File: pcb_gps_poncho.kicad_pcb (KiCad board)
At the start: 2 copper layers, 41.9 x 61 mm, 9 parts, among them P1 CONN_5, P2 CONN_4

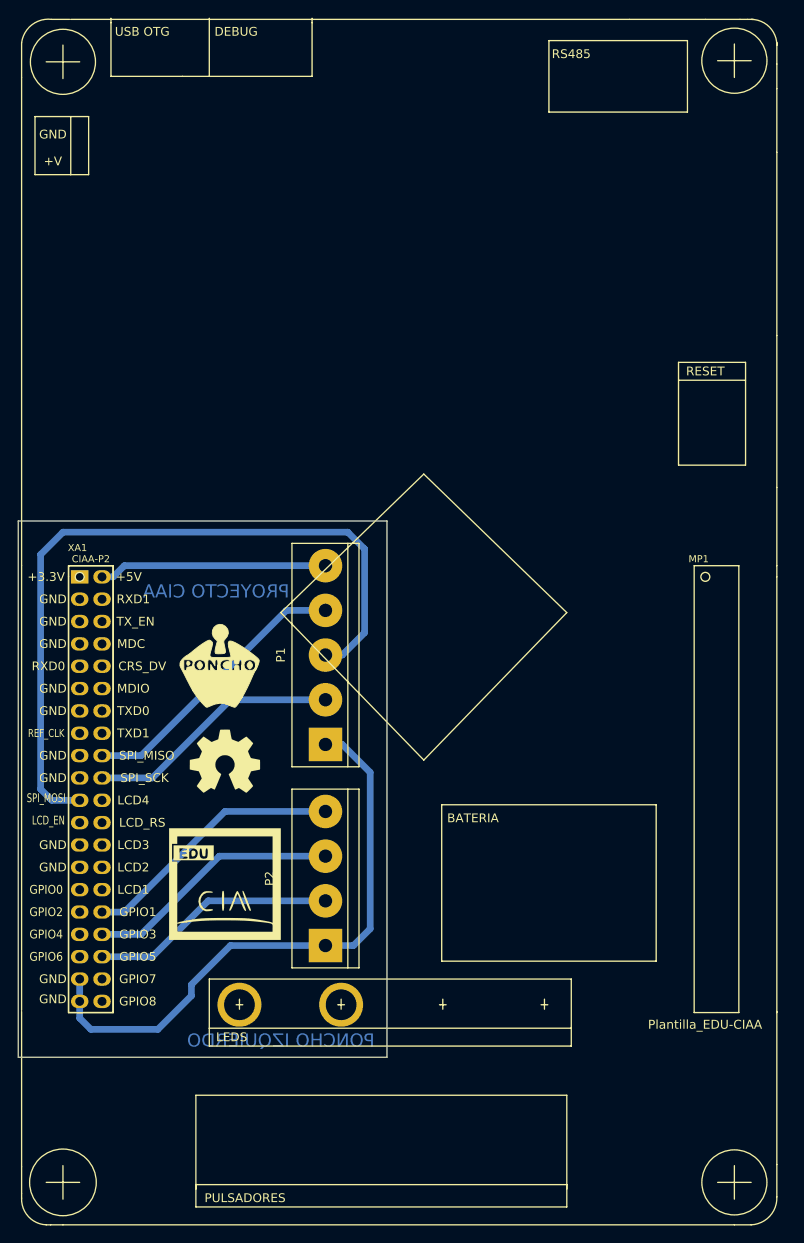
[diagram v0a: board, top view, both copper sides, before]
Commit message: Cambio de chip gps y modelo de poncho
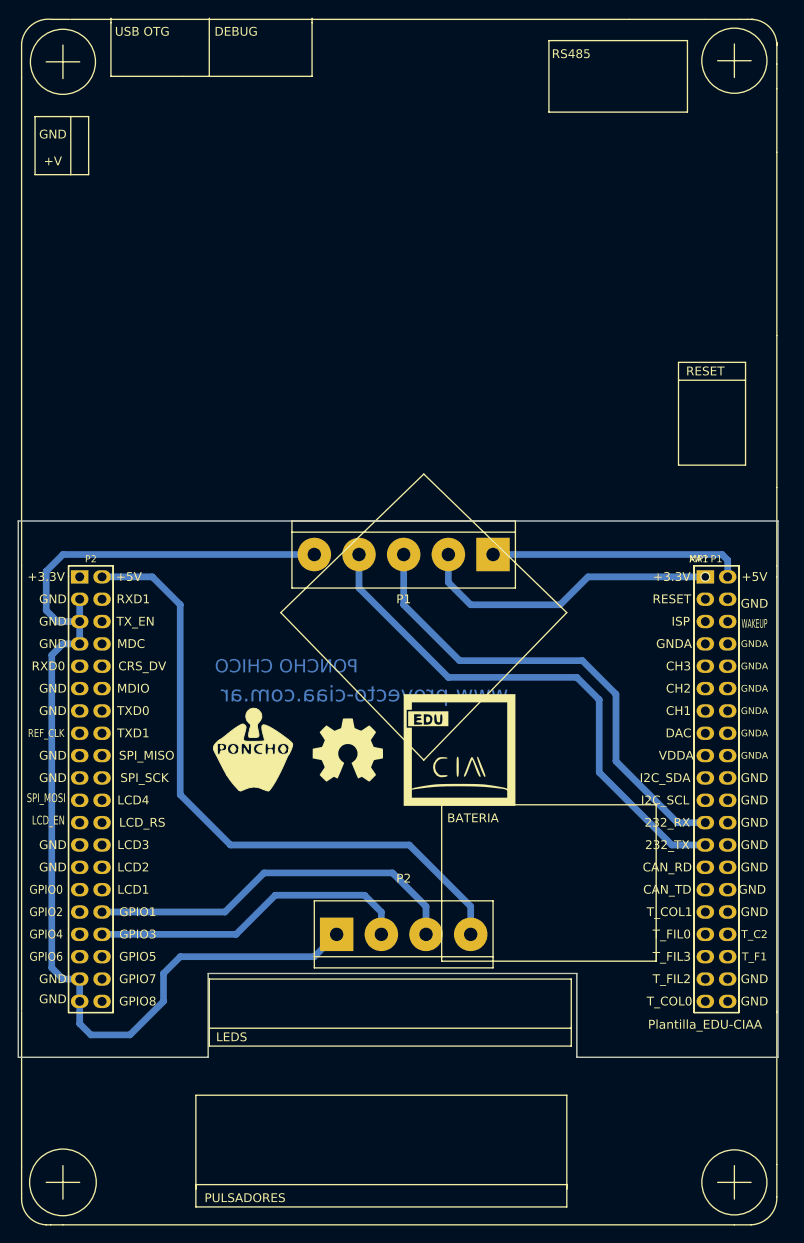
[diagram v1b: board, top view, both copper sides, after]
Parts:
- removed H1, H2: PCB_HOLE, Poncho_Modelos:Led_Hole
- removed MP1: Plantilla_EDU-CIAA, Poncho_Esqueleto:Plantilla_EDU-CIAA
- added MP?: Plantilla_EDU-CIAA, Poncho_Esqueleto:Plantilla_EDU-CIAA, F.Cu at (142.2, 81.3)
- XA1: footprint Poncho_Esqueleto:Conn_Poncho_Izquierdo -> Poncho_Esqueleto:Conn_Poncho_Chico
- moved XA1 71.1 mm to (142.2, 81.3)
- moved G*** 30.7 mm to (114.3, 101.0)
- moved P1 14.5 mm to (108.0, 78.7), turned to 180 degrees
- moved G101 14.0 mm to (101.6, 101.0)
- moved P2 10.9 mm to (108.0, 121.9), turned to 0 degrees
- moved G*** 10.3 mm to (90.8, 101.0)
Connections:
- P1 pad 1: GND -> +5V
- P1 pad 2: Net-(P1-Pad2) -> +3.3V
- P1 pad 5: +5VP -> GND
- P2 pad 4: Net-(P2-Pad4) -> +5VP
- XA1 pad 43: (no net) -> GND
- XA1 pad 45: (no net) -> GND
- XA1 pad 47: (no net) -> GND
- XA1 pad 58: Net-(P1-Pad4) -> (no net)
- XA1 pad 60: Net-(P1-Pad2) -> (no net)
- XA1 pad 61: Net-(P1-Pad3) -> (no net)
- XA1 pad 72: Net-(P2-Pad4) -> Net-(P2-Pad3)
- XA1 pad 74: Net-(P2-Pad3) -> Net-(P2-Pad2)
- XA1 pad 76: Net-(P2-Pad2) -> (no net)
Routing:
- net GND: track 67.6 -> 130.8 mm
- net +5VP: track 25.9 -> 73.3 mm
- net +3.3V: track 0.00 -> 34.8 mm
- net Net-(P1-Pad3): track 85.3 -> 54.7 mm
- net Net-(P2-Pad4): track 30.1 -> 0.00 mm
- net Net-(P1-Pad2): track 29.1 -> 0.00 mm
- net +5V: track 0.00 -> 28.8 mm
- net Net-(P1-Pad4): track 32.2 -> 60.1 mm
- net Net-(P2-Pad3): track 29.1 -> 43.4 mm
- net Net-(P2-Pad2): track 28.0 -> 36.9 mm
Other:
- board size 41.9 x 61 mm -> 86.4 x 61 mm
- board text added: "PONCHO CHICO"
- board text added: "PONCHO CHICO http://www.proyecto-ciaa.com.ar/"
- board text added: "www.proyecto-ciaa.com.ar"
- board text removed: "PONCHO IZQUIERDO"
- board text removed: "PONCHO IZQUIERDO http://www.proyecto-ciaa.com.ar/"
- board text removed: "PROYECTO CIAA"
